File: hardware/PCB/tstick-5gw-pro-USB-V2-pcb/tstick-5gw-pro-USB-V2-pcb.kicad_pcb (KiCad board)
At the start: 4 copper layers, 55.9 x 25.2 mm, 51 parts, among them J1 USB_C_Receptacle_USB2.0, J2 GPIO2, J3 GPIO1, Q3 BSS138, SW1 JST-SH-1.00mm 1x2, SW2 PTS810 SJM Switch, SW3 PTS810 SJM Switch, U1 max8819ceti+, U4 PCA9306DP

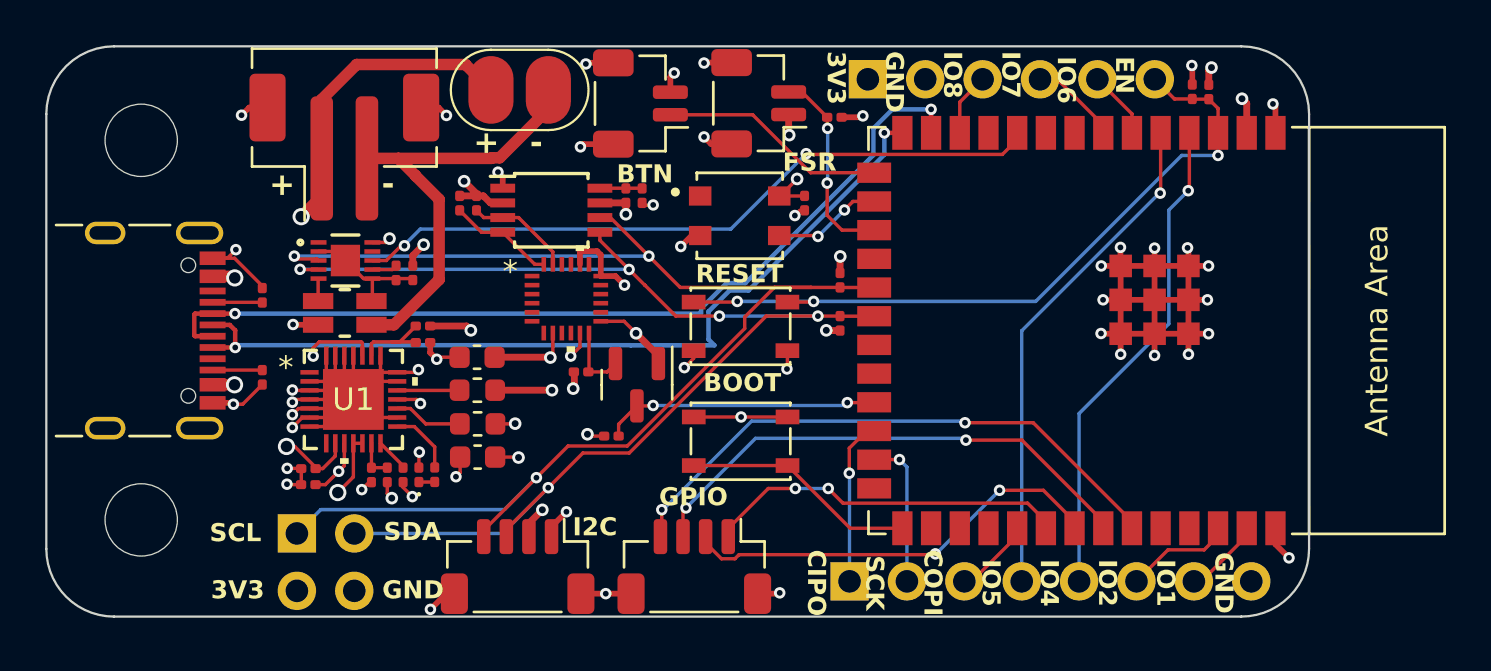
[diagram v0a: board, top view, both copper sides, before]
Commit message: added thermistor
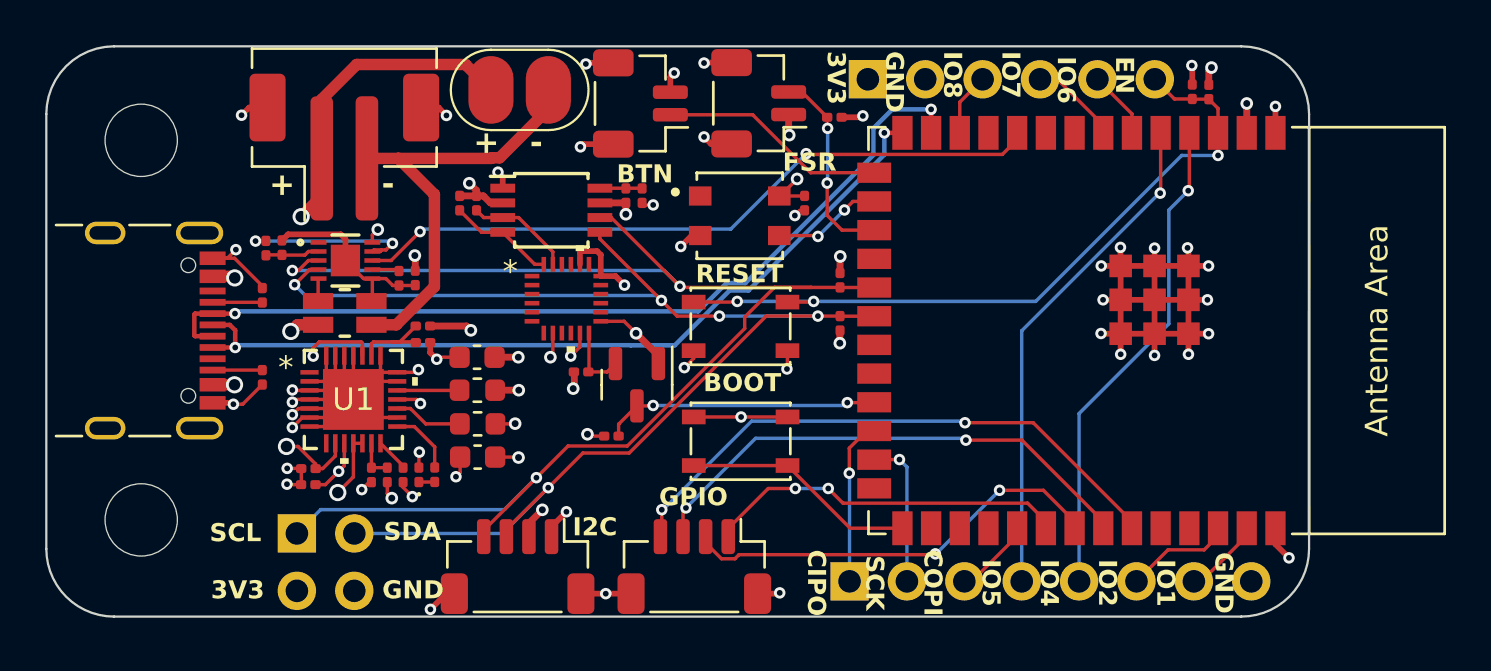
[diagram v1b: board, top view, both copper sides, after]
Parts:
- added R12: 10k, Resistor_SMD:R_0201_0603Metric, F.Cu at (108.8, 56.8)
- added TH1: 10k, Resistor_SMD:R_0201_0603Metric, F.Cu at (109.5, 56.8)
- moved C2 0.27 mm to (114.6, 58.1)
- moved C1 0.25 mm to (115.4, 58.1)
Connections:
- FG1 pad 2: CSP -> /AIN
- FG1 pad 9: unconnected-(FG1-THRM-Pad9) -> /THRM
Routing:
- net /THRM: track 0.00 -> 8.03 mm, vias 0 -> 2
- net +1V8: track 15.1 -> 12.0 mm, vias 6 -> 7
- net CSP: track 5.71 -> 8.52 mm
- net /SDA: track 56.7 -> 59.1 mm
- net /AIN: track 0.00 -> 2.41 mm
- net /SCL: track 61.4 -> 63.3 mm
- net /USBD+: track 38.1 -> 36.9 mm

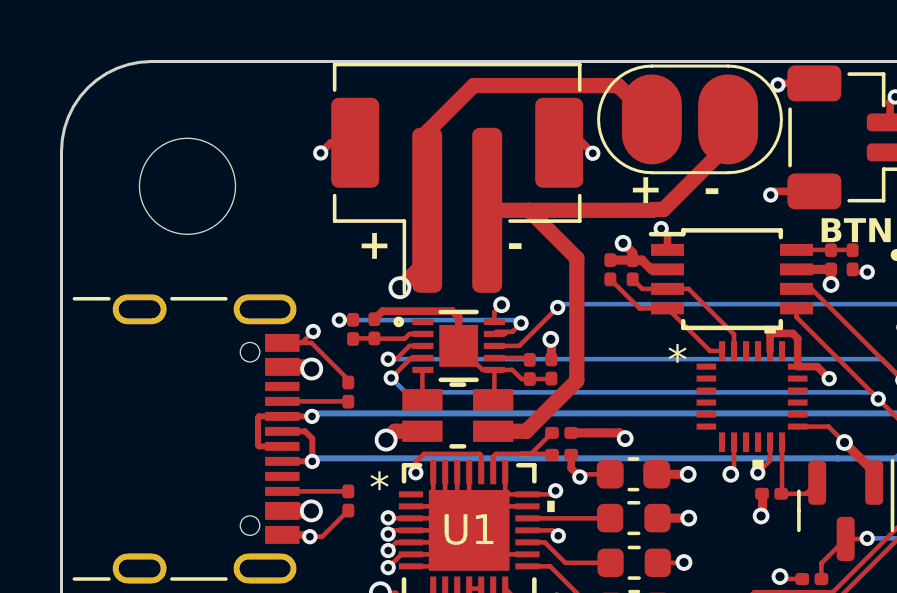
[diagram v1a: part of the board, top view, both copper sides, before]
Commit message: cleaned up v1 of the boards, fixed issue with evt2 trace not being connected in touch board
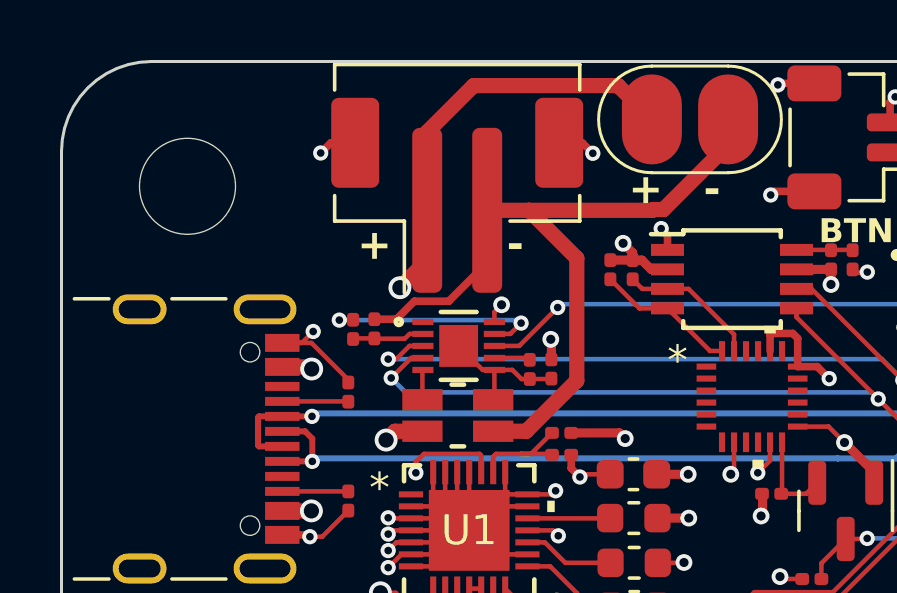
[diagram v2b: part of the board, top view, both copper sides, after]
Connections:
- TH1 pad 2: CSP -> -BATT
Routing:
- net -BATT: track 19.6 -> 25.9 mm
- net CSP: track 8.52 -> 4.57 mm
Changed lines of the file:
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@@
     (property "Sheetfile" "tstick-5gw-pro-USB-V2-pcb.kicad_sch")
     (property "Sheetname" "")
+    (property "exclude_from_bom" "")
     (property "ki_description" "Generic connector, single row, 01x08, script generated (kicad-library-utils/schlib/autogen/connector/)")
     (property "ki_keywords" "connector")
-    (attr through_hole)
+    (attr through_hole exclude_from_bom)
     (fp_text reference "J3" (at 0 -2.33 90) (layer "F.SilkS") hide
         (effects (font (size 1 1) (thickness 0.15)))
@@
       (net 84 "/AIN") (pintype "passive"))
     (pad "2" smd roundrect (at 0.32 0 90) (size 0.46 0.4) (layers "F.Cu" "F.Mask") (roundrect_rratio 0.25)
-      (net 3 "CSP") (pintype "passive"))
+      (net 2 "-BATT") (pintype "passive"))
     (model "${KICAD6_3DMODEL_DIR}/Resistor_SMD.3dshapes/R_0201_0603Metric.wrl"
       (offset (xyz 0 0 0))
@@
     (property "Sheetfile" "tstick-5gw-pro-USB-V2-pcb.kicad_sch")
     (property "Sheetname" "")
+    (property "exclude_from_bom" "")
     (property "ki_description" "Generic connector, single row, 01x06, script generated (kicad-library-utils/schlib/autogen/connector/)")
     (property "ki_keywords" "connector")
-    (attr through_hole)
+    (attr through_hole exclude_from_bom)
     (fp_text reference "J2" (at 0 -2.33 90) (layer "F.SilkS") hide
         (effects (font (size 1 1) (thickness 0.15)))
@@
   (segment (start 118.729145 52.83) (end 118.756145 52.803) (width 0.508) (layer "F.Cu") (net 2))
   (segment (start 113.22 52.83) (end 114.61 52.83) (width 0.508) (layer "F.Cu") (net 2))
+  (segment (start 110.193947 56.46) (end 110.793947 55.86) (width 0.254) (layer "F.Cu") (net 2))
   (segment (start 118.756145 52.803) (end 119.097 52.803) (width 0.508) (layer "F.Cu") (net 2))
   (segment (start 114.521935 60.195) (end 113.4199 60.195) (width 0.508) (layer "F.Cu") (net 2))
@@
   (segment (start 121.25 50.65) (end 121.25 49.8) (width 0.508) (layer "F.Cu") (net 2))
   (segment (start 114.61 52.83) (end 116.207 54.427) (width 0.508) (layer "F.Cu") (net 2))
+  (segment (start 109.46 56.46) (end 110.193947 56.46) (width 0.254) (layer "F.Cu") (net 2))
   (segment (start 114.61 52.83) (end 118.729145 52.83) (width 0.508) (layer "F.Cu") (net 2))
+  (segment (start 111.94 55.86) (end 113.22 54.58) (width 0.254) (layer "F.Cu") (net 2))
+  (segment (start 113.22 54.58) (end 113.22 52.83) (width 0.254) (layer "F.Cu") (net 2))
   (segment (start 119.097 52.803) (end 121.25 50.65) (width 0.508) (layer "F.Cu") (net 2))
+  (segment (start 110.793947 55.86) (end 111.94 55.86) (width 0.254) (layer "F.Cu") (net 2))
   (segment (start 116.207 58.509935) (end 114.521935 60.195) (width 0.508) (layer "F.Cu") (net 2))
   (segment (start 113.46 58.150002) (end 113.46 59.1049) (width 0.1524) (layer "F.Cu") (net 3))
@@
   (segment (start 113.46 59.1049) (end 113.4199 59.145) (width 0.1524) (layer "F.Cu") (net 3))
   (segment (start 115.345 58.455) (end 115.36 58.44) (width 0.1524) (layer "F.Cu") (net 3))
-  (segment (start 112.063099 56.192) (end 112.2686 56.397501) (width 0.254) (layer "F.Cu") (net 3))
   (segment (start 113.46 58.150002) (end 114.060002 58.150002) (width 0.1524) (layer "F.Cu") (net 3))
-  (segment (start 112.2686 56.397501) (end 112.2686 57.350001) (width 0.254) (layer "F.Cu") (net 3))
   (segment (start 113.46 58.150002) (end 113.068601 58.150002) (width 0.1524) (layer "F.Cu") (net 3))
   (segment (start 113.068601 58.150002) (end 112.2686 57.350001) (width 0.1524) (layer "F.Cu") (net 3))
-  (segment (start 109.728 56.192) (end 112.063099 56.192) (width 0.254) (layer "F.Cu") (net 3))
   (segment (start 114.060002 58.150002) (end 114.365 58.455) (width 0.1524) (layer "F.Cu") (net 3))
-  (segment (start 109.46 56.46) (end 109.728 56.192) (width 0.254) (layer "F.Cu") (net 3))
   (segment (start 114.64 58.455) (end 115.345 58.455) (width 0.1524) (layer "F.Cu") (net 3))
   (segment (start 121.448401 61.521099) (end 121.34 61.6295) (width 0.1524) (layer "F.Cu") (net 4))
@@
   (segment (start 111.0601 58.167102) (end 111.0772 58.150002) (width 0.1524) (layer "F.Cu") (net 13))
   (segment (start 111.0601 59.145) (end 111.0601 58.167102) (width 0.1524) (layer "F.Cu") (net 13))
-  (segment (start 114.35 56.59) (end 114.0594 56.8806) (width 0.1524) (layer "F.Cu") (net 15))
   (segment (start 108.75 56.48) (end 108.3 56.48) (width 0.1524) (layer "F.Cu") (net 15))
-  (segment (start 114.0594 56.8806) (end 113.529402 56.8806) (width 0.1524) (layer "F.Cu") (net 15))
   (segment (start 108.3 56.48) (end 108.29 56.49) (width 0.1524) (layer "F.Cu") (net 15))
-  (segment (start 113.810519 56.950002) (end 113.866425 56.894096) (width 0.1524) (layer "F.Cu") (net 15))
-  (segment (start 113.529402 56.8806) (end 113.46 56.950002) (width 0.1524) (layer "F.Cu") (net 15))
+  (segment (start 113.989998 56.950002) (end 113.46 56.950002) (width 0.1524) (layer "F.Cu") (net 15))
+  (segment (start 114.35 56.59) (end 113.989998 56.950002) (width 0.1524) (layer "F.Cu") (net 15))
   (segment (start 113.46 56.950002) (end 113.810519 56.950002) (width 0.1524) (layer "F.Cu") (net 15))
   (via (at 114.35 56.59) (size 0.508) (drill 0.254) (layers "F.Cu" "B.Cu") (net 15))
